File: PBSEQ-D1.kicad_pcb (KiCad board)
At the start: 2 copper layers, 19 x 19 mm, 25 parts, among them J1 POWER IN, J2 POWER OUT, J3 BUTTON, Q1 AO3401A, Q2 AO3400A, SW1 BUTTON

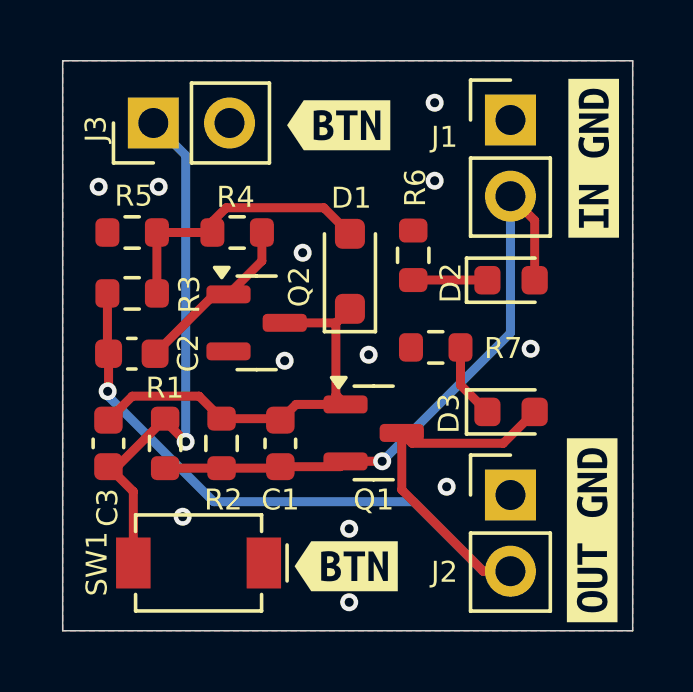
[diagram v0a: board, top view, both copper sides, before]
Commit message: R0.2
* Fixed the diode connection issue. The Cathode was connected to the wrong point.
* Updated `Q1` to AO3415.
* The circuit has been tested and working.
* Updated all 0603 footprints to hand-soldering type for easy soldering.
* Rearranged the silkscreen labels.
* DRC passes.
* Updated BoM.
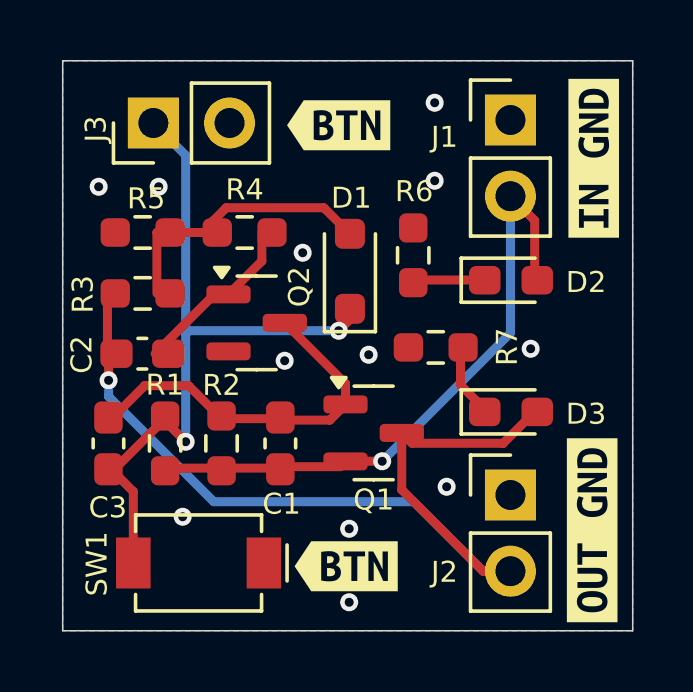
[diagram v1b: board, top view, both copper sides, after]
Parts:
- removed kibuzzard-66404F66: G***, kibuzzard-66404F66
- added kibuzzard-665C27BB: G***, kibuzzard-665C27BB, B.Cu at (135.0, 99.3)
- C1, C2, C3: footprint Capacitor_SMD:C_0603_1608Metric -> Capacitor_SMD:C_0603_1608Metric_Pad1.08x0.95mm_HandSolder
- D2, D3: footprint LED_SMD:LED_0603_1608Metric -> LED_SMD:LED_0603_1608Metric_Pad1.05x0.95mm_HandSolder
- Q1: value AO3401A -> AO3415
- R1, R2, R3, R4, R5, R6, R7: footprint Resistor_SMD:R_0603_1608Metric -> Resistor_SMD:R_0603_1608Metric_Pad0.98x0.95mm_HandSolder
- moved C2 0.35 mm to (132.7, 100.8)
- moved R3 0.35 mm to (132.7, 98.8)
- moved R5 0.35 mm to (132.7, 96.7)
- moved R4 0.25 mm to (136.1, 96.7)
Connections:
- C1 pad 2: Net-(D1-K) -> Net-(Q1-G)
- C3 pad 1: Net-(D1-K) -> Net-(Q1-G)
- C3 pad 2: Net-(J3-Pin_1) -> Net-(D1-K)
- J3 pad 1: Net-(J3-Pin_1) -> Net-(D1-K)
- Q1 pad 1: Net-(D1-K) -> Net-(Q1-G)
- Q2 pad 3: Net-(D1-K) -> Net-(Q1-G)
- R1 pad 1: Net-(J3-Pin_1) -> Net-(D1-K)
- R2 pad 2: Net-(D1-K) -> Net-(Q1-G)
- SW1 pad 2: Net-(J3-Pin_1) -> Net-(D1-K)
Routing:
- net Net-(J3-Pin_1): track 18.2 -> 0.00 mm, vias 1 -> 0
- net Net-(Q1-G): track 0.00 -> 12.6 mm
- net Net-(D1-K): track 14.0 -> 24.3 mm, vias 0 -> 2
